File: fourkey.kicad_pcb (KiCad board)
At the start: 2 copper layers, 85.3 x 75.7 mm, 23 parts, among them K1 KEYSW, K2 KEYSW, K3 KEYSW, K4 KEYSW, SW1 SW_PUSH, U1 ProMicro

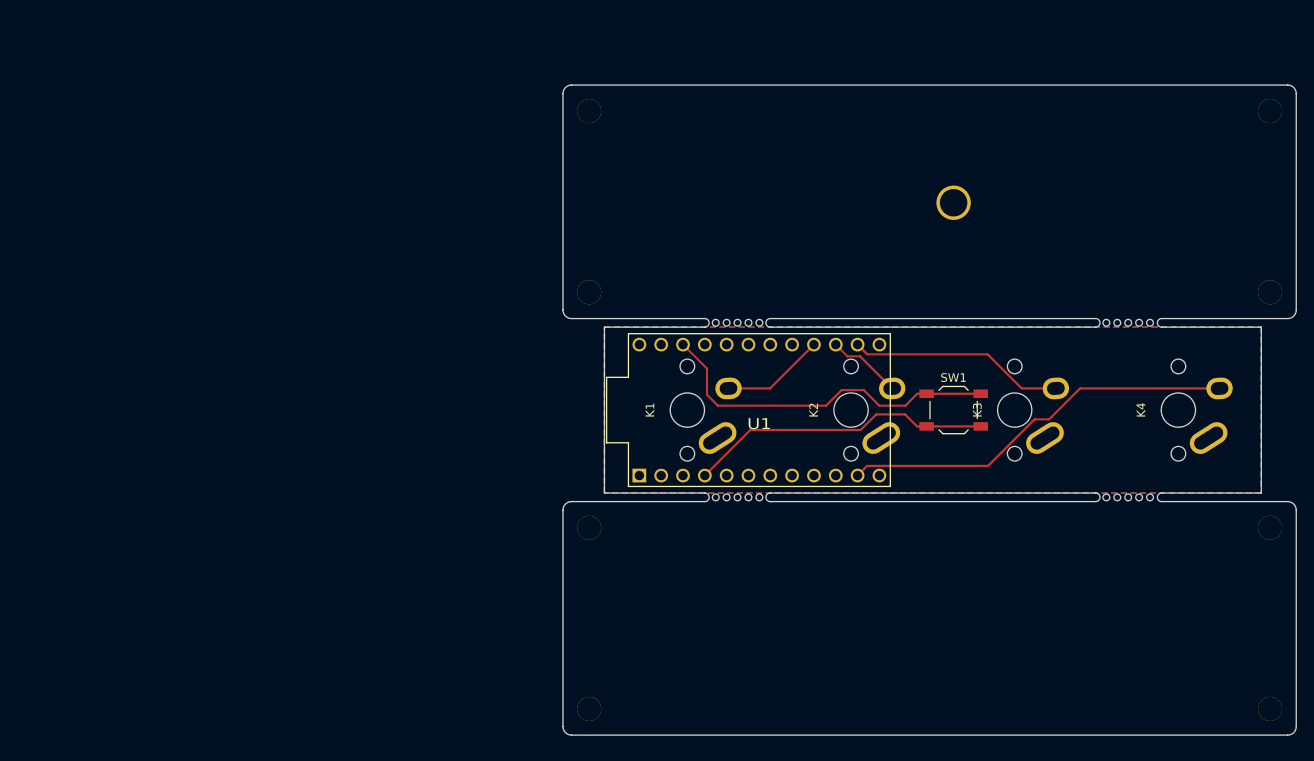
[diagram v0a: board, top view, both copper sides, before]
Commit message: move mousebites
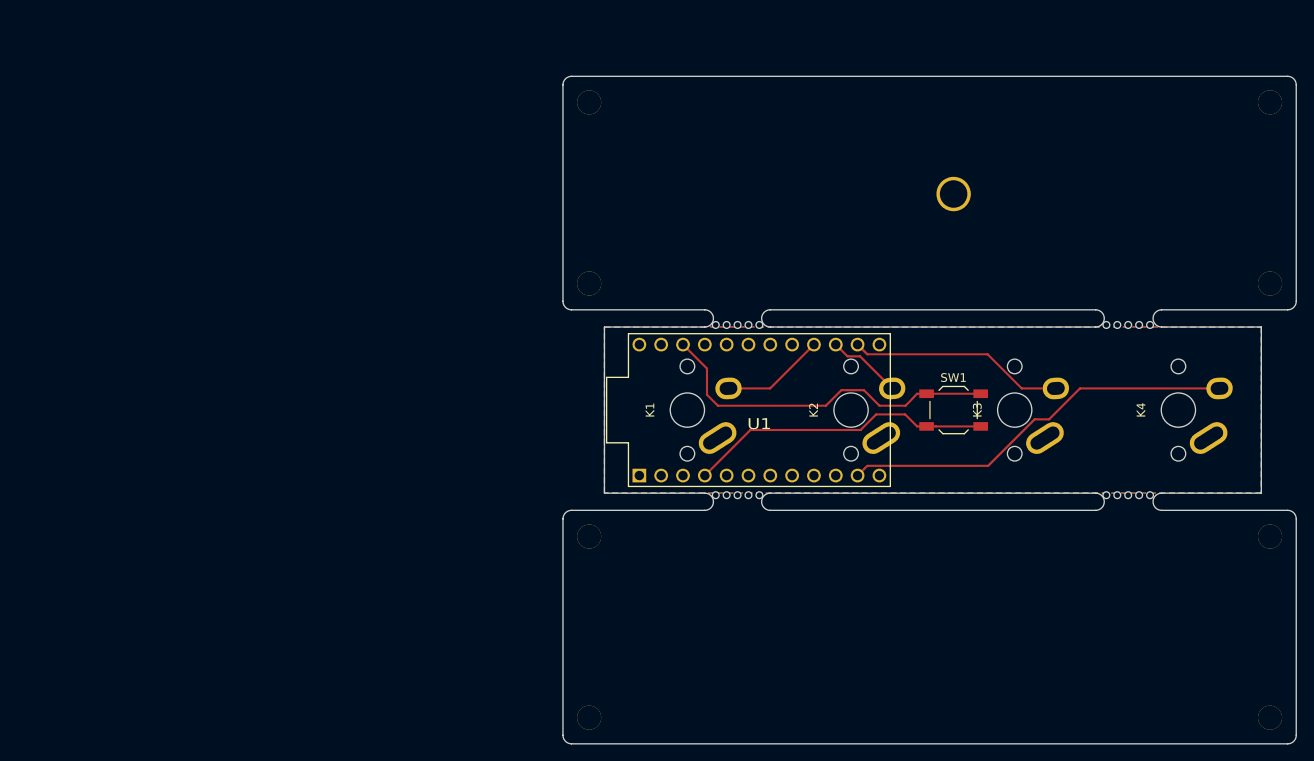
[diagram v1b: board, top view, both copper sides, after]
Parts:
- removed the HOLE_M2.6 at (130.0, 121.1)
- removed the HOLE_M2.6 at (209.3, 121.1)
- removed the HOLE_M2.6 at (130.0, 100.1)
- removed the HOLE_M2.6 at (209.3, 100.1)
- removed the HOLE_M2.6 at (130.0, 72.6)
- removed the HOLE_M2.6 at (130.0, 51.6)
- removed the HOLE_M2.6 at (209.3, 51.6)
- removed the HOLE_M2.6 at (209.3, 72.6)
- removed the REF** at (147.3, 76.5)
- removed the REF** at (192.8, 76.5)
- removed the REF** at (192.8, 96.8)
- removed the REF** at (147.3, 96.8)
- removed the REF** at (198.6, 110.5)
- removed the REF** at (179.6, 110.5)
- removed the REF** at (160.5, 110.5)
- removed the REF** at (141.5, 110.5)
- added HOLE_M2.6: VAL**, keyboard_parts:HOLE_M2.6, B.Cu at (130.0, 122.2)
- added HOLE_M2.6: VAL**, keyboard_parts:HOLE_M2.6, B.Cu at (209.3, 122.2)
- added HOLE_M2.6: VAL**, keyboard_parts:HOLE_M2.6, B.Cu at (130.0, 101.1)
- added HOLE_M2.6: VAL**, keyboard_parts:HOLE_M2.6, B.Cu at (209.3, 101.1)
- added HOLE_M2.6: VAL**, keyboard_parts:HOLE_M2.6, F.Cu at (130.0, 71.6)
- added HOLE_M2.6: VAL**, keyboard_parts:HOLE_M2.6, F.Cu at (130.0, 50.5)
- added HOLE_M2.6: VAL**, keyboard_parts:HOLE_M2.6, F.Cu at (209.3, 50.5)
- added HOLE_M2.6: VAL**, keyboard_parts:HOLE_M2.6, F.Cu at (209.3, 71.6)
- added REF**: breakaway-mousebites, Keebio-Parts:breakaway-mousebites, F.Cu at (147.3, 76.7)
- added REF**: breakaway-mousebites, Keebio-Parts:breakaway-mousebites, F.Cu at (192.8, 76.7)
- added REF**: breakaway-mousebites, Keebio-Parts:breakaway-mousebites, F.Cu at (192.8, 96.0)
- added REF**: breakaway-mousebites, Keebio-Parts:breakaway-mousebites, F.Cu at (147.3, 96.0)
- added REF**: MX_Switch_Cutout, Keebio-Parts:MX_Switch_Cutout, F.Cu at (198.6, 111.5)
- added REF**: MX_Switch_Cutout, Keebio-Parts:MX_Switch_Cutout, F.Cu at (179.6, 111.5)
- added REF**: MX_Switch_Cutout, Keebio-Parts:MX_Switch_Cutout, F.Cu at (160.5, 111.5)
- added REF**: MX_Switch_Cutout, Keebio-Parts:MX_Switch_Cutout, F.Cu at (141.5, 111.5)
- moved HOLE_M3 1.02 mm to (172.5, 61.2)
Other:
- board size 85.3 x 75.7 mm -> 85.3 x 77.7 mm

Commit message: sign the pcb
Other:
- board text added: "github.com/trepmal/fourkey"
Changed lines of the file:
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@@
   (general
     (thickness 1.6)
-    (drawings 36)
+    (drawings 37)
     (tracks 38)
     (zones 0)
@@
   (page A4)
   (layers
-    (0 F.Cu signal hide)
-    (31 B.Cu signal hide)
+    (0 F.Cu signal)
+    (31 B.Cu signal)
     (32 B.Adhes user)
     (33 F.Adhes user)
@@
     )
   )
+  (gr_text github.com/trepmal/fourkey (at 158.496 61.214) (layer B.SilkS)
+    (effects (font (size 1 1) (thickness 0.15)) (justify mirror))
+  )
   (gr_arc (start 211.344 73.692) (end 212.344 73.692) (angle 90) (layer Edge.Cuts) (width 0.05))

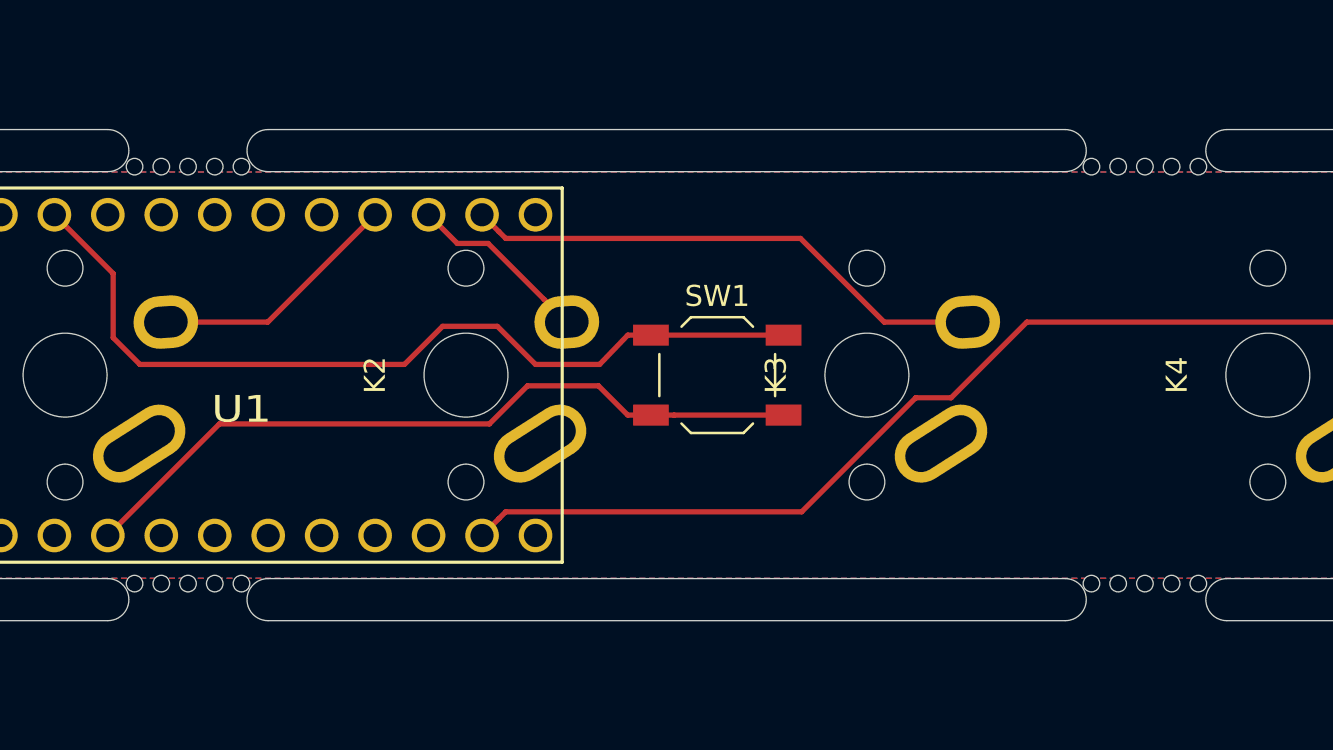
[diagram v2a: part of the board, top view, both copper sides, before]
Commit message: extra mousebites
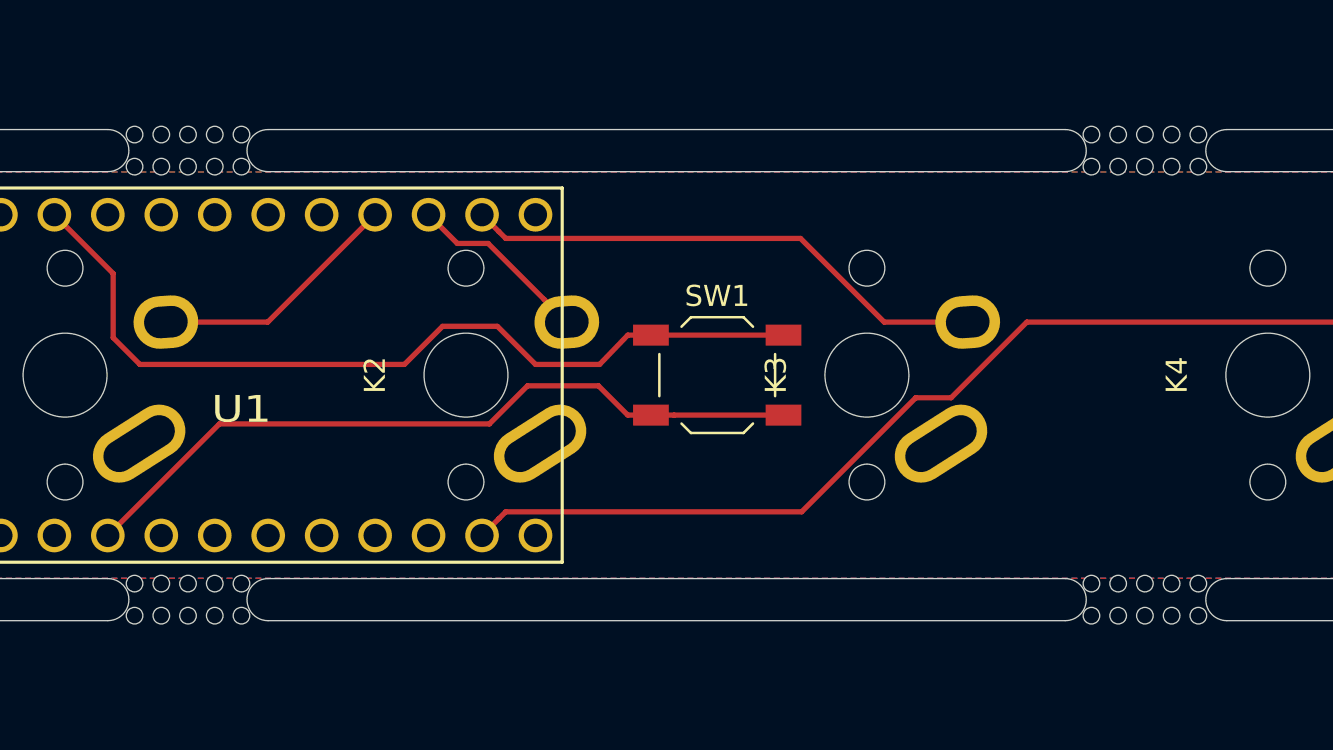
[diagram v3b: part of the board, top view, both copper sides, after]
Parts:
- added REF**: breakaway-mousebites, Keebio-Parts:breakaway-mousebites, F.Cu at (147.3, 98.0)
- added REF**: breakaway-mousebites, Keebio-Parts:breakaway-mousebites, F.Cu at (192.8, 98.0)
- added REF**: breakaway-mousebites, Keebio-Parts:breakaway-mousebites, F.Cu at (192.8, 74.7)
- added REF**: breakaway-mousebites, Keebio-Parts:breakaway-mousebites, F.Cu at (147.3, 74.7)
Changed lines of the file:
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@@
     (tracks 38)
     (zones 0)
-    (modules 23)
+    (modules 27)
     (nets 27)
   )
@@
   )
   (module Keebio-Parts:breakaway-mousebites (layer F.Cu)
+    (at 147.32 98.044)
+    (fp_text reference REF** (at 0 -3.048) (layer Dwgs.User) hide
+      (effects (font (size 1 1) (thickness 0.15)))
+    )
+    (fp_text value breakaway-mousebites (at 0 -4.75) (layer F.Fab) hide
+      (effects (font (size 1 1) (thickness 0.15)))
+    )
+    (fp_line (start -2.794 0) (end 2.794 0) (layer Dwgs.User) (width 0.15))
+    (pad "" np_thru_hole circle (at 0 -0.254) (size 0.7874 0.7874) (drill 0.7874) (layers *.Cu *.Mask))
+    (pad "" np_thru_hole circle (at 1.27 -0.254) (size 0.7874 0.7874) (drill 0.7874) (layers *.Cu *.Mask))
+    (pad "" np_thru_hole circle (at 2.54 -0.254) (size 0.7874 0.7874) (drill 0.7874) (layers *.Cu *.Mask))
+    (pad "" np_thru_hole circle (at -1.27 -0.254) (size 0.7874 0.7874) (drill 0.7874) (layers *.Cu *.Mask))
+    (pad "" np_thru_hole circle (at -2.54 -0.254) (size 0.7874 0.7874) (drill 0.7874) (layers *.Cu *.Mask))
+  )
+  (module Keebio-Parts:breakaway-mousebites (layer F.Cu)
+    (at 192.786 98.044)
+    (fp_text reference REF** (at 0 -3.048) (layer Dwgs.User) hide
+      (effects (font (size 1 1) (thickness 0.15)))
+    )
+    (fp_text value breakaway-mousebites (at 0 -4.75) (layer F.Fab) hide
+      (effects (font (size 1 1) (thickness 0.15)))
+    )
+    (fp_line (start -2.794 0) (end 2.794 0) (layer Dwgs.User) (width 0.15))
+    (pad "" np_thru_hole circle (at 0 -0.254) (size 0.7874 0.7874) (drill 0.7874) (layers *.Cu *.Mask))
+    (pad "" np_thru_hole circle (at 1.27 -0.254) (size 0.7874 0.7874) (drill 0.7874) (layers *.Cu *.Mask))
+    (pad "" np_thru_hole circle (at 2.54 -0.254) (size 0.7874 0.7874) (drill 0.7874) (layers *.Cu *.Mask))
+    (pad "" np_thru_hole circle (at -1.27 -0.254) (size 0.7874 0.7874) (drill 0.7874) (layers *.Cu *.Mask))
+    (pad "" np_thru_hole circle (at -2.54 -0.254) (size 0.7874 0.7874) (drill 0.7874) (layers *.Cu *.Mask))
+  )
+  (module Keebio-Parts:breakaway-mousebites (layer F.Cu)
+    (at 192.786 74.676 180)
+    (fp_text reference REF** (at 0 -3.048) (layer Dwgs.User) hide
+      (effects (font (size 1 1) (thickness 0.15)))
+    )
+    (fp_text value breakaway-mousebites (at 0 -4.75) (layer F.Fab) hide
+      (effects (font (size 1 1) (thickness 0.15)))
+    )
+    (fp_line (start -2.794 0) (end 2.794 0) (layer Dwgs.User) (width 0.15))
+    (pad "" np_thru_hole circle (at 0 -0.254 180) (size 0.7874 0.7874) (drill 0.7874) (layers *.Cu *.Mask))
+    (pad "" np_thru_hole circle (at 1.27 -0.254 180) (size 0.7874 0.7874) (drill 0.7874) (layers *.Cu *.Mask))
+    (pad "" np_thru_hole circle (at 2.54 -0.254 180) (size 0.7874 0.7874) (drill 0.7874) (layers *.Cu *.Mask))
+    (pad "" np_thru_hole circle (at -1.27 -0.254 180) (size 0.7874 0.7874) (drill 0.7874) (layers *.Cu *.Mask))
+    (pad "" np_thru_hole circle (at -2.54 -0.254 180) (size 0.7874 0.7874) (drill 0.7874) (layers *.Cu *.Mask))
+  )
+  (module Keebio-Parts:breakaway-mousebites (layer F.Cu)
+    (at 147.32 74.676 180)
+    (fp_text reference REF** (at 0 -3.048) (layer Dwgs.User) hide
+      (effects (font (size 1 1) (thickness 0.15)))
+    )
+    (fp_text value breakaway-mousebites (at 0 -4.75) (layer F.Fab) hide
+      (effects (font (size 1 1) (thickness 0.15)))
+    )
+    (fp_line (start -2.794 0) (end 2.794 0) (layer Dwgs.User) (width 0.15))
+    (pad "" np_thru_hole circle (at 0 -0.254 180) (size 0.7874 0.7874) (drill 0.7874) (layers *.Cu *.Mask))
+    (pad "" np_thru_hole circle (at 1.27 -0.254 180) (size 0.7874 0.7874) (drill 0.7874) (layers *.Cu *.Mask))
+    (pad "" np_thru_hole circle (at 2.54 -0.254 180) (size 0.7874 0.7874) (drill 0.7874) (layers *.Cu *.Mask))
+    (pad "" np_thru_hole circle (at -1.27 -0.254 180) (size 0.7874 0.7874) (drill 0.7874) (layers *.Cu *.Mask))
+    (pad "" np_thru_hole circle (at -2.54 -0.254 180) (size 0.7874 0.7874) (drill 0.7874) (layers *.Cu *.Mask))
+  )
+  (module Keebio-Parts:breakaway-mousebites (layer F.Cu)

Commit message: hide labels
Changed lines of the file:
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@@
     (descr MXALPS)
     (tags MXALPS)
-    (fp_text reference K1 (at 0 -4.318 90) (layer F.SilkS)
+    (fp_text reference K1 (at 0 -4.318 90) (layer F.SilkS) hide
       (effects (font (size 1 1) (thickness 0.2)))
     )
@@
     (descr "Pro Micro footprint")
     (tags "promicro ProMicro")
-    (fp_text reference U1 (at 0 1.625) (layer F.SilkS)
+    (fp_text reference U1 (at 0 1.625) (layer F.SilkS) hide
       (effects (font (size 1.27 1.524) (thickness 0.2032)))
     )
@@
     (descr MXALPS)
     (tags MXALPS)
-    (fp_text reference K2 (at 0 -4.318 90) (layer F.SilkS)
+    (fp_text reference K2 (at 0 -4.318 90) (layer F.SilkS) hide
       (effects (font (size 1 1) (thickness 0.2)))
     )
@@
     (descr MXALPS)
     (tags MXALPS)
-    (fp_text reference K3 (at 0 -4.318 90) (layer F.SilkS)
+    (fp_text reference K3 (at 0 -4.318 90) (layer F.SilkS) hide
       (effects (font (size 1 1) (thickness 0.2)))
     )
@@
     (descr MXALPS)
     (tags MXALPS)
-    (fp_text reference K4 (at 0 -4.318 90) (layer F.SilkS)
+    (fp_text reference K4 (at 0 -4.318 90) (layer F.SilkS) hide
       (effects (font (size 1 1) (thickness 0.2)))
     )
@@
     (tags "SPST Tactile Switch")
     (attr smd)
-    (fp_text reference SW1 (at 0 -3.75) (layer F.SilkS)
+    (fp_text reference SW1 (at 0 -3.75) (layer F.SilkS) hide
       (effects (font (size 1 1) (thickness 0.15)))
     )

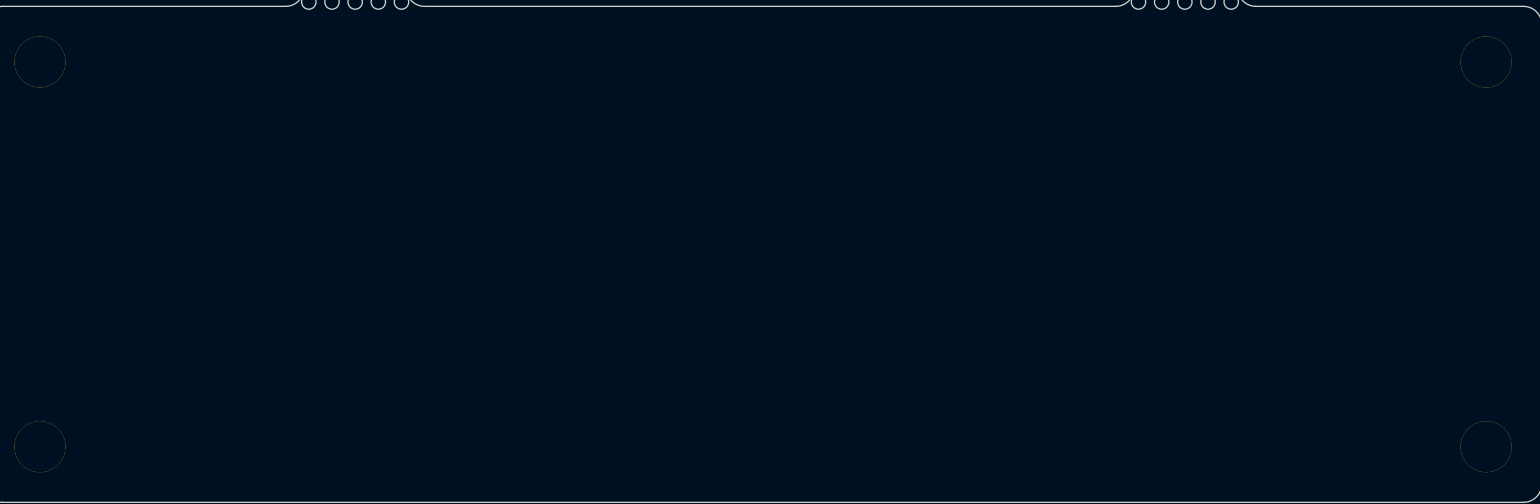
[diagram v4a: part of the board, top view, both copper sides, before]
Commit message: replace switch cutouts with cleaner edgecuts
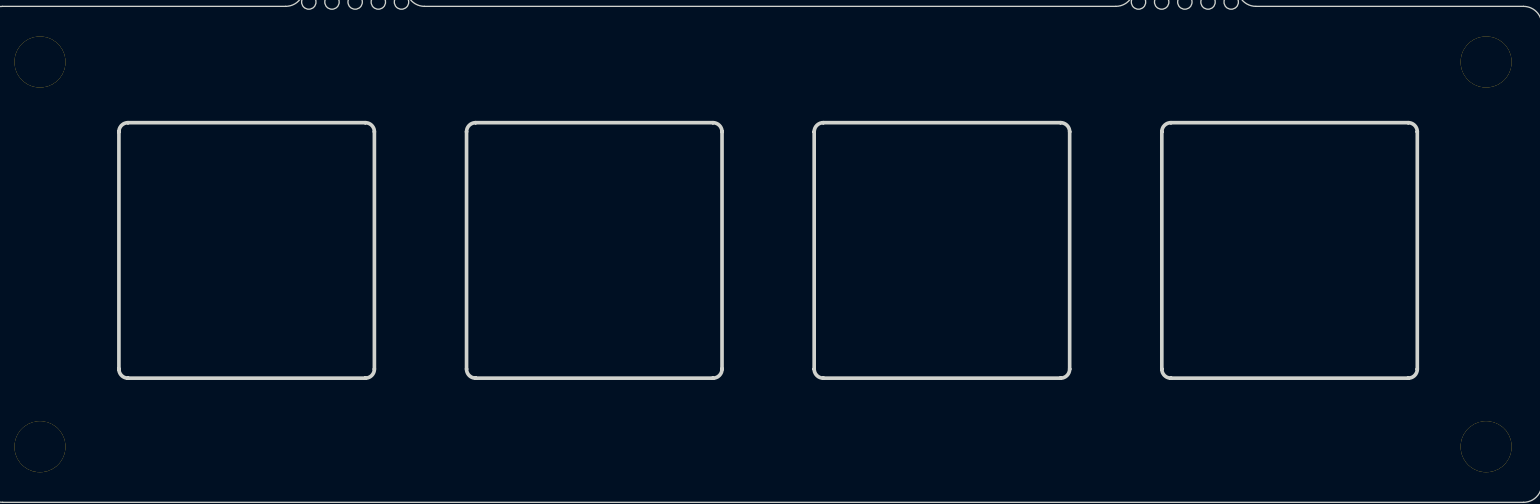
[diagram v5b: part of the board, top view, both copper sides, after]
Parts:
- removed the REF** at (179.6, 111.5)
- removed the REF** at (160.5, 111.5)
- removed the REF** at (141.5, 111.5)
- removed the REF** at (198.6, 111.5)
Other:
- outline, holes or cut-outs redrawn
